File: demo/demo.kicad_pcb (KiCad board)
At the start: 2 copper layers, 32 parts, among them SW1 SW_Push, SW10 SW_Push, SW11 SW_Push, SW12 SW_Push, SW13 SW_Push, SW14 SW_Push, SW15 SW_Push, SW16 SW_Push, SW2 SW_Push, SW3 SW_Push, SW4 SW_Push, SW5 SW_Push, SW6 SW_Push, SW7 SW_Push, SW8 SW_Push, SW9 SW_Push

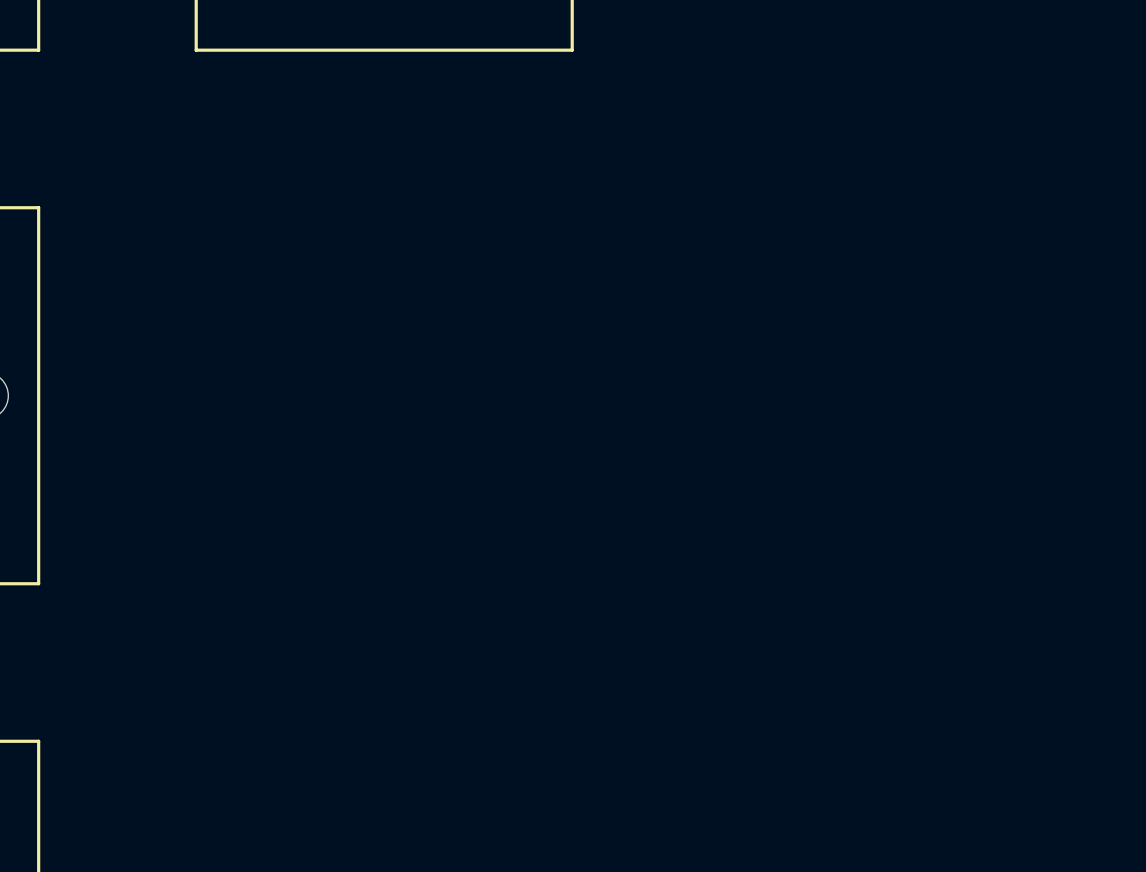
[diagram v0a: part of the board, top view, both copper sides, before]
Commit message: Add addressable RGB LEDs to demo board
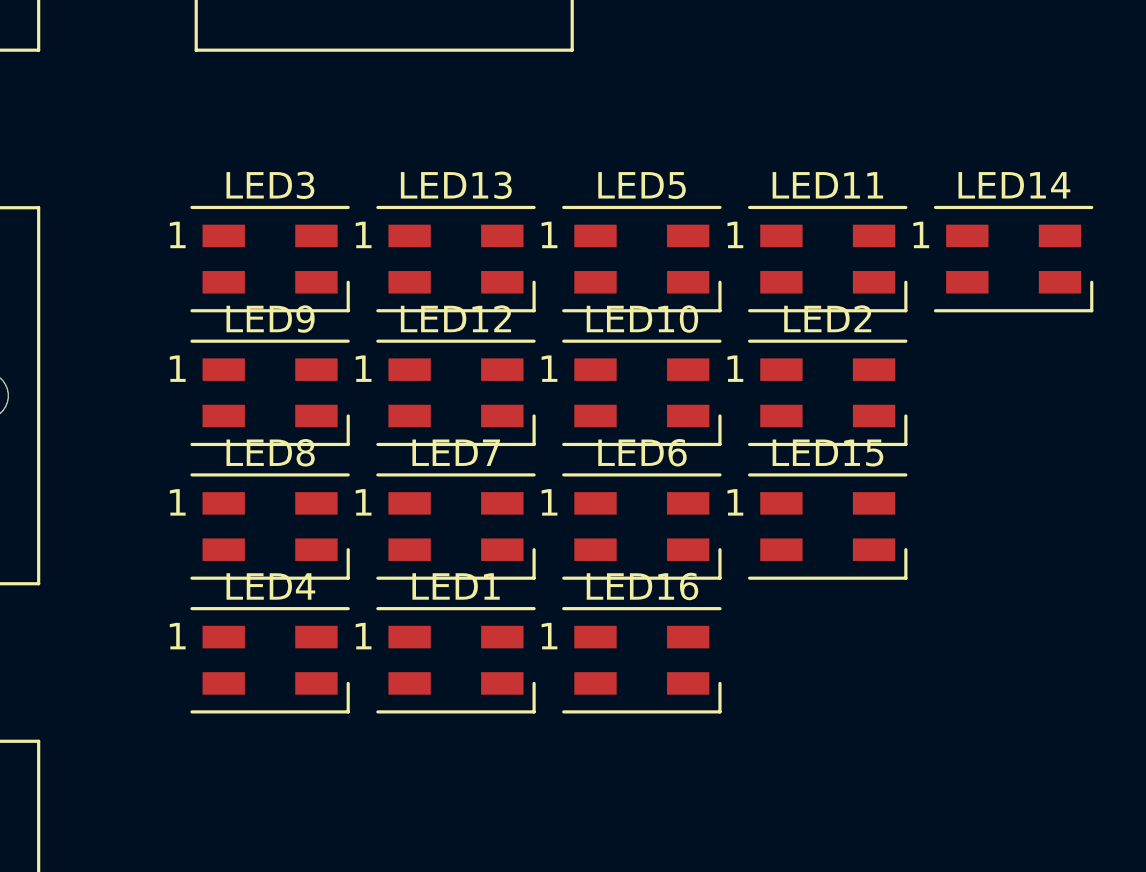
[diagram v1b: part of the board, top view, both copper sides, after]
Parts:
- added LED1: SK6812MINI, LED_SMD:LED_SK6812MINI_PLCC4_3.5x3.5mm_P1.75mm, F.Cu at (111.8, -35.6)
- added LED10: SK6812MINI, LED_SMD:LED_SK6812MINI_PLCC4_3.5x3.5mm_P1.75mm, F.Cu at (118.8, -45.7)
- added LED11: SK6812MINI, LED_SMD:LED_SK6812MINI_PLCC4_3.5x3.5mm_P1.75mm, F.Cu at (125.8, -50.7)
- added LED12: SK6812MINI, LED_SMD:LED_SK6812MINI_PLCC4_3.5x3.5mm_P1.75mm, F.Cu at (111.8, -45.7)
- added LED13: SK6812MINI, LED_SMD:LED_SK6812MINI_PLCC4_3.5x3.5mm_P1.75mm, F.Cu at (111.8, -50.7)
- added LED14: SK6812MINI, LED_SMD:LED_SK6812MINI_PLCC4_3.5x3.5mm_P1.75mm, F.Cu at (132.8, -50.7)
- added LED15: SK6812MINI, LED_SMD:LED_SK6812MINI_PLCC4_3.5x3.5mm_P1.75mm, F.Cu at (125.8, -40.6)
- added LED16: SK6812MINI, LED_SMD:LED_SK6812MINI_PLCC4_3.5x3.5mm_P1.75mm, F.Cu at (118.8, -35.6)
- added LED2: SK6812MINI, LED_SMD:LED_SK6812MINI_PLCC4_3.5x3.5mm_P1.75mm, F.Cu at (125.8, -45.7)
- added LED3: SK6812MINI, LED_SMD:LED_SK6812MINI_PLCC4_3.5x3.5mm_P1.75mm, F.Cu at (104.7, -50.7)
- added LED4: SK6812MINI, LED_SMD:LED_SK6812MINI_PLCC4_3.5x3.5mm_P1.75mm, F.Cu at (104.7, -35.6)
- added LED5: SK6812MINI, LED_SMD:LED_SK6812MINI_PLCC4_3.5x3.5mm_P1.75mm, F.Cu at (118.8, -50.7)
- added LED6: SK6812MINI, LED_SMD:LED_SK6812MINI_PLCC4_3.5x3.5mm_P1.75mm, F.Cu at (118.8, -40.6)
- added LED7: SK6812MINI, LED_SMD:LED_SK6812MINI_PLCC4_3.5x3.5mm_P1.75mm, F.Cu at (111.8, -40.6)
- added LED8: SK6812MINI, LED_SMD:LED_SK6812MINI_PLCC4_3.5x3.5mm_P1.75mm, F.Cu at (104.7, -40.6)
- added LED9: SK6812MINI, LED_SMD:LED_SK6812MINI_PLCC4_3.5x3.5mm_P1.75mm, F.Cu at (104.7, -45.7)
